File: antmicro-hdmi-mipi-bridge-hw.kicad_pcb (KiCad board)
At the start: 4 copper layers, 68 x 45 mm, 123 parts, among them IC1 TLV73325PDBVT, IC2 TLV73312PDBVT, IC3 TLV73325PDBVT, IC4 TLV73312PDBVT, J2 47151-1001, J3 5051101992, J4 47151-1001, J5 5051101992, J6 WE_68715014022, U1 TC358742XBG, U2 TPD8S009DSMR, U3 PCA9517ATP, U4 TC358742XBG, U5 TPD8S009DSMR, U6 PCA9517ATP, Y1 7C-27.000MBB-T, Y2 7C-27.000MBB-T

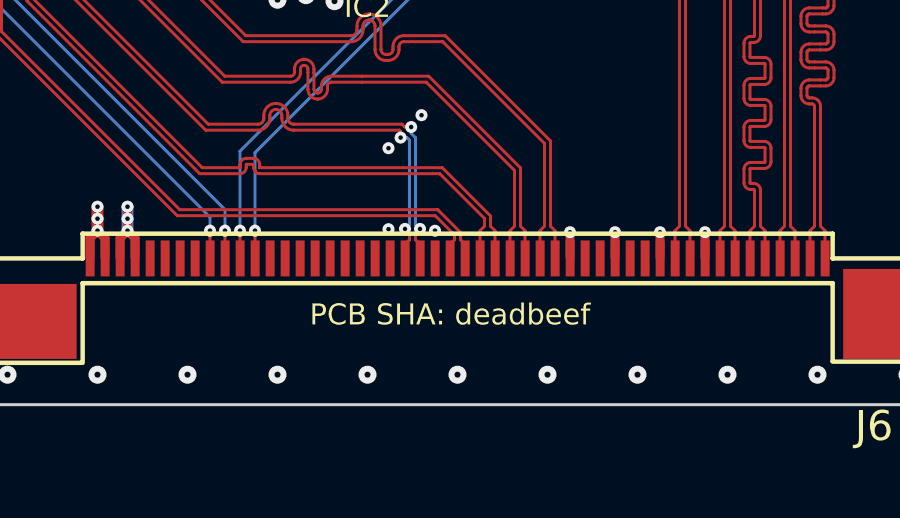
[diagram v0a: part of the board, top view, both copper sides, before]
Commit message: Update PCB marking strings
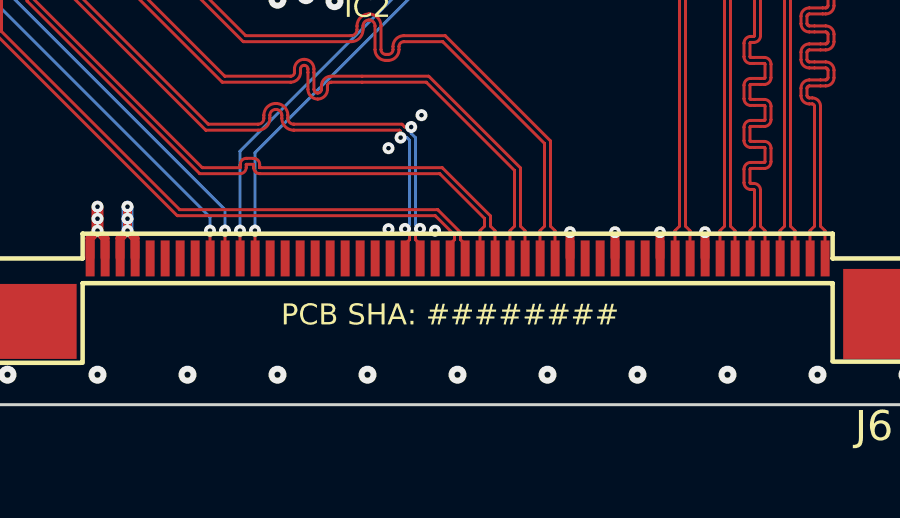
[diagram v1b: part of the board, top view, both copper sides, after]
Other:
- board text added: "PCB SHA: ########"
- board text removed: "PCB SHA deadbeef"
- board text removed: "PCB SHA: deadbeef"
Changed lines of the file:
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@@
   (gr_line (start 159.8 119.35) (end 159.15 119.35) (layer "F.SilkS") (width 0.15))
   (gr_rect (start 115 90) (end 183 135) (layer "Edge.Cuts") (width 0.1) (fill none))
-  (gr_text "PCB SHA deadbeef" (at 149 132) (layer "B.SilkS")
+  (gr_text "PCB SHA: ########" (at 149 132) (layer "B.SilkS")
     (effects (font (size 0.65 0.65) (thickness 0.15)) (justify mirror))
   )
-  (gr_text "PCB SHA: deadbeef" (at 148.75 132) (layer "F.SilkS")
+  (gr_text "PCB SHA: ########" (at 148.75 132) (layer "F.SilkS")
     (effects (font (size 0.7 0.7) (thickness 0.15)))
   )

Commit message: Update local library of components
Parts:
- C1, C12, C13, C14, C15, C16, C2, C21, C22, C23, C24, C25, C26, C27, C28, C29, C3, C30, C31, C32, C33, C34, C35, C36, C37, C38, C39, C4, C44, C45, C46, C47, C48, C49, C5, C50, C6, C7: footprint antmicro-footprints:0402-cap -> antmicro-hdmi-mipi-bridge-hw-footprints:0402-cap
- C10, C11, C17, C18, C19, C20, C40, C41, C42, C43, C51, C52, C53, C54, C8, C9: footprint antmicro-footprints:0603-cap -> antmicro-hdmi-mipi-bridge-hw-footprints:0603-cap
- FB1, FB7, R1, R14, R15, R18, R19, R2, R20, R21, R5, R6, R7, R8: footprint antmicro-footprints:0603-res -> antmicro-hdmi-mipi-bridge-hw-footprints:0603-res
- FB10, FB11, FB2, FB3, FB4, FB5, FB8, FB9: footprint antmicro-footprints:0805-res -> antmicro-hdmi-mipi-bridge-hw-footprints:0805-res
- FB12, FB6: footprint antmicro-footprints:0603 -> antmicro-hdmi-mipi-bridge-hw-footprints:0603
- G***: footprint antmicro-footprints:antmicro-logo_scaled_20mm_mask -> antmicro-hdmi-mipi-bridge-hw-footprints:antmicro-logo_scaled_20mm_mask
- IC1, IC2, IC3, IC4: footprint antmicro-footprints:SOT-23-5 -> antmicro-hdmi-mipi-bridge-hw-footprints:SOT-23-5
- J2, J4: footprint antmicro-footprints:47151-1001 -> antmicro-hdmi-mipi-bridge-hw-footprints:47151-1001
- J3, J5: footprint antmicro-footprints:5051101992 -> antmicro-hdmi-mipi-bridge-hw-footprints:5051101992
- J6: footprint antmicro-footprints:WE_68715014022 -> antmicro-hdmi-mipi-bridge-hw-footprints:WE_68715014022
- R10, R11, R12, R13, R16, R17, R22, R23, R24, R25, R26, R3, R4, R9: footprint antmicro-footprints:0402-res -> antmicro-hdmi-mipi-bridge-hw-footprints:0402-res
- REF**: footprint antmicro-footprints:OSHW-Symbol_6.7x6mm_Mask -> antmicro-hdmi-mipi-bridge-hw-footprints:OSHW-Symbol_6.7x6mm_Mask
- SP1, SP2, SP3, SP4: footprint antmicro-footprints:9774060151 -> antmicro-hdmi-mipi-bridge-hw-footprints:9774060151
- TP1, TP2, TP3, TP4, TP5, TP6, TP7, TP8: footprint antmicro-footprints:Testpoint_smd_0_75mm -> antmicro-hdmi-mipi-bridge-hw-footprints:Testpoint_smd_0_75mm
- U1, U4: footprint antmicro-footprints:BGA-64_8x8_6.0x6.0mm -> antmicro-hdmi-mipi-bridge-hw-footprints:BGA-64_8x8_6.0x6.0mm
- U2, U5: footprint antmicro-footprints:R-PDSO-N15 -> antmicro-hdmi-mipi-bridge-hw-footprints:R-PDSO-N15
- U3, U6: footprint antmicro-footprints:SOT1069-2 -> antmicro-hdmi-mipi-bridge-hw-footprints:SOT1069-2
- Y1, Y2: footprint antmicro-footprints:7C-24.000MBB-T -> antmicro-hdmi-mipi-bridge-hw-footprints:7C-24.000MBB-T
